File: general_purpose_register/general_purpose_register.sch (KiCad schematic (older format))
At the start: 38 parts, among them J1 Power, J2 Control, J3 Data Bus, J4 ALU LHS, J5 ALU RHS, U1 74HCT574, U2 74HCT541, U3 74HCT541, U4 74HCT541

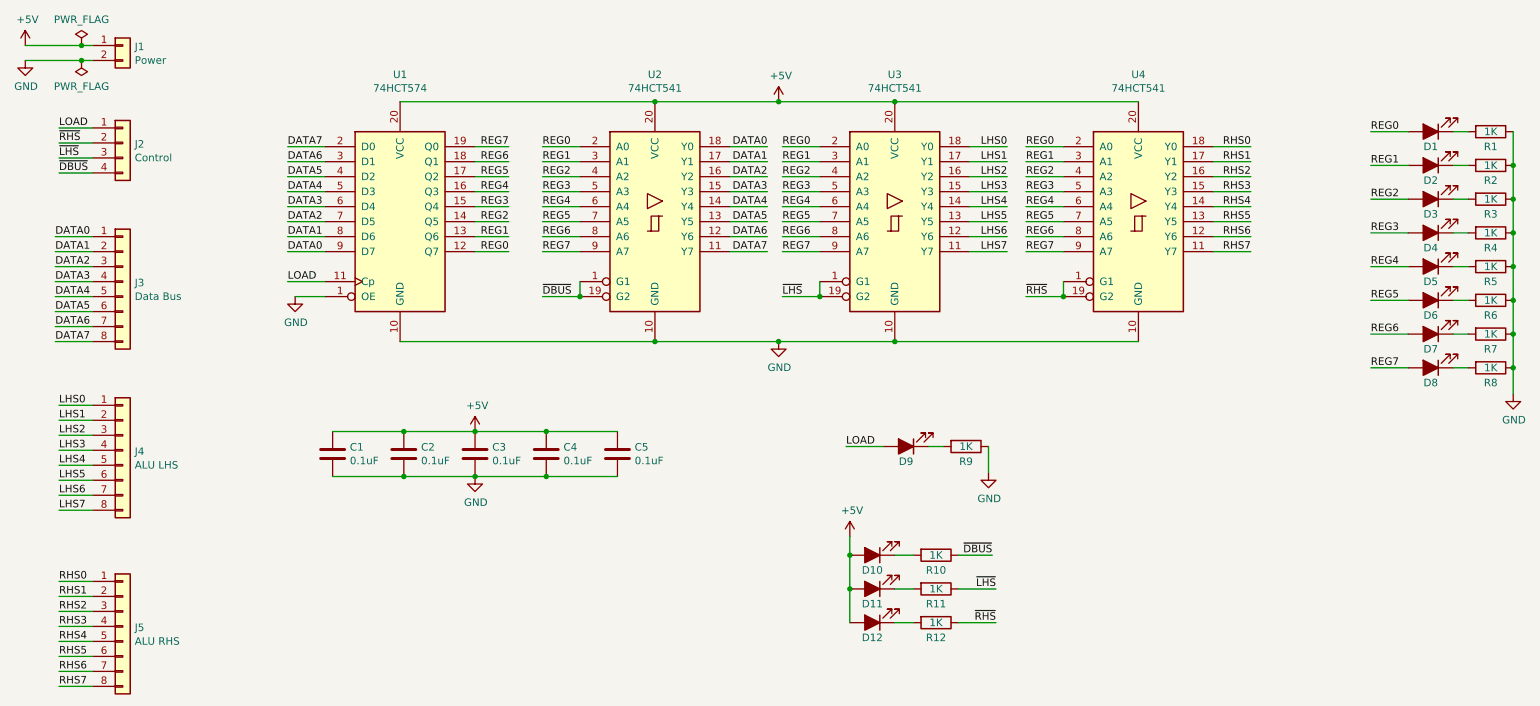
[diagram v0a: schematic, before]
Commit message: Rerouted for better ground plane.
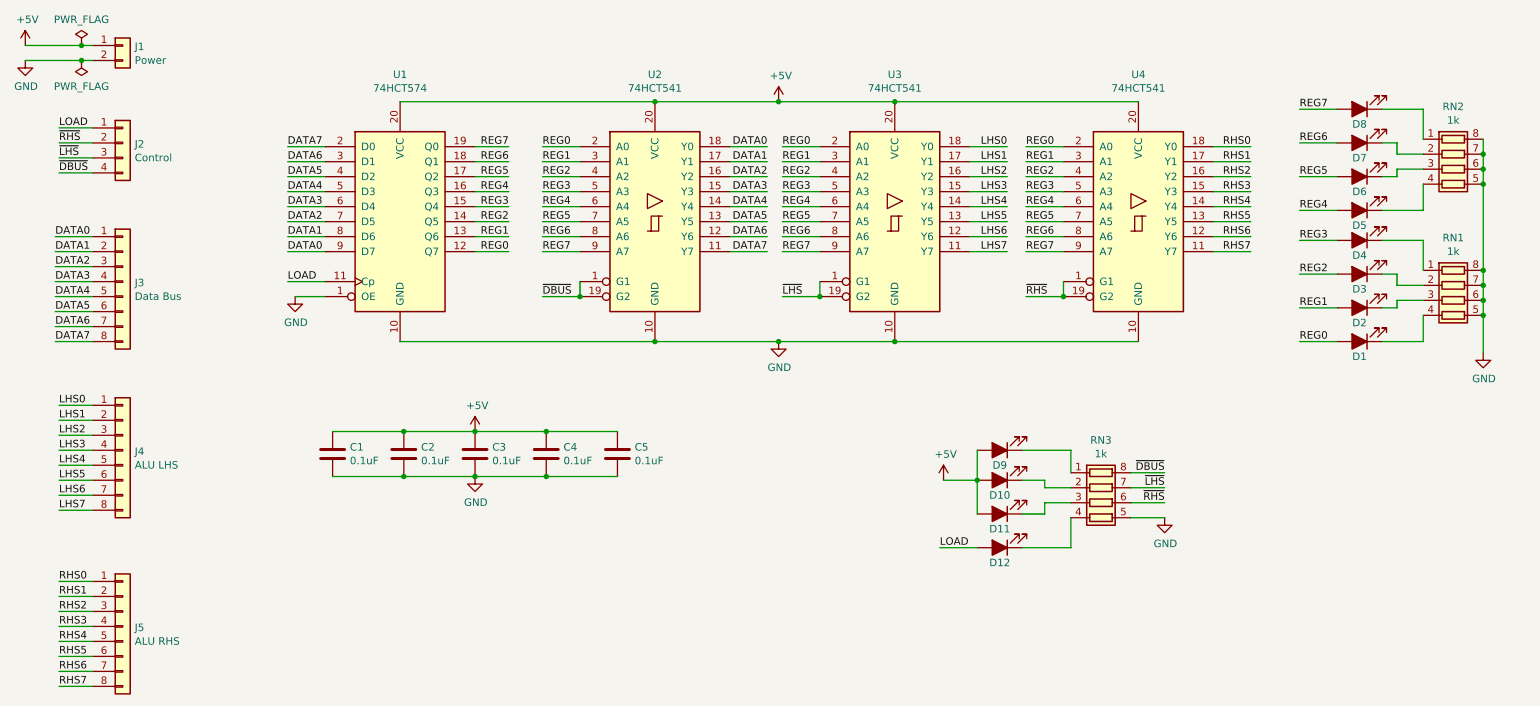
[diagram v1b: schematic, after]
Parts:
- removed R1, R10, R11, R12, R2, R3, R4, R5, R6, R7, R8, R9: 1K, Resistor_SMD:R_0805_2012Metric_Pad1.20x1.40mm_HandSolder, symbol Device:R
- added RN1, RN2, RN3: 1k, Resistor_SMD:R_Array_Convex_4x1206, symbol Device:R_Pack04
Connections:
- net +5V: now also D9.2 (A); no longer D12.2 (A)
- net GND: now also RN1.5 (R4.2), RN1.6 (R3.2), RN1.7 (R2.2), RN1.8 (R1.2), RN2.5 (R4.2), RN2.6 (R3.2), RN2.7 (R2.2), RN2.8 (R1.2), RN3.5 (R4.2)
- net LOAD: now also D12.2 (A); no longer D9.2 (A)
- net ~DBUS: now also RN3.8 (R1.2)
- net ~LHS: now also RN3.7 (R2.2)
- net ~RHS: now also RN3.6 (R3.2)
- net at D1.1 (K): now also RN1.4 (R4.1)
- net at D2.1 (K): now also RN1.3 (R3.1)
- net at D3.1 (K): now also RN1.2 (R2.1)
- net at D4.1 (K): now also RN1.1 (R1.1)
- net at D5.1 (K): now also RN2.4 (R4.1)
- net at D6.1 (K): now also RN2.3 (R3.1)
- net at D7.1 (K): now also RN2.2 (R2.1)
- net at D8.1 (K): now also RN2.1 (R1.1)
- net at D9.1 (K): now also RN3.1 (R1.1)
- net at D10.1 (K): now also RN3.2 (R2.1)
- net at D11.1 (K): now also RN3.3 (R3.1)
- net at D12.1 (K): now also RN3.4 (R4.1)
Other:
- moved on the sheet: D1, D10, D11, D12, D2, D3, D4, D5, D6, D7, D8, D9
